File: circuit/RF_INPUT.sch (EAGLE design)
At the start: 90 parts, among them IC1 TS464, IC2 SN74LVC1G3157DBVR, U1 SA612, U2 SA612, U3 SA612, X1 BU-SMA-V, X4 SMA-142-0701-801/806, X5 BU-SMA-V, X6 SMA-142-0701-801/806

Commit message: - развели половину
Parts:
- removed C37: nc, rcl:C-EUC0603
- removed R10: 680K, rcl:R-EU_R0603
- C1, C10, C11, C15, C18, C19, C20, C21, C22, C23, C26, C31, C32, C33, C34, C4, C6, C7, C8: device rcl:C-EUC0603 -> rcl:C-EUC0805
- C24: value 220N -> 100N
- C25: value nc -> 220N; device rcl:C-EUC0603 -> rcl:C-EUC0805
- R11: value 680K -> 330K
- R41: value 150K -> 330k
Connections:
- removed net LO_RX: U3.OSCB
- new net N$3: C25.2, U3.OSCB
- net +6V0: no longer R10.2
- net GND: now also C24.1; no longer C24.2, C25.2, C37.2, R11.2
- net LO_TX: now also C25.1
- net N$47: no longer C37.1
- net N$59: no longer C25.1
- net N$73: no longer R10.1
- net OPA_BIAS: now also C24.2, R11.2; no longer C24.1
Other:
- moved on the sheet: C24, C25, R11

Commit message: - почти разведенная схема
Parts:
- added Q1, Q2: IRML6302, transistor-small-signal:BSS84
- added R10, R42: 4.7k, rcl:R-EU_R0603
- added R43, R44: 68k, rcl:R-EU_R0603
- added R45: 220, rcl:R-EU_R0603
- added X8: (no value), con-phoenix-254:MPT2
- C30: device rcl:C-EUC0603 -> rcl:C-EUC0805
- R14, R19, R2, R21, R3: device rcl:R-EU_R0603 -> rcl:R-EU_R0805
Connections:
- new net N$10: R10.1, X8-1.1
- new net N$11: IC2.B2, R45.2
- new net N$4: C26.1, C27.1, Q2.D, U3.VCC
- new net N$6: Q1.G, R10.2, R43.2
- new net N$7: Q2.G, R42.2, R44.2
- new net N$8: C15.1, C16.1, Q1.D, U2.VCC
- new net N$9: R42.1, X8-2.1
- net +6V0: now also Q1.S, Q2.S, R43.1, R44.1; no longer C15.1, C16.1, C26.1, C27.1, U2.VCC, U3.VCC
- net ADC_SWITCH_CNTRL: now also IC2.A; no longer R36.2
- net ADC_SWITCH_NC: now also IC1A.OUT, R45.1; no longer IC1B.OUT, IC2.B2
- net ADC_SWITCH_NO: now also R36.1; no longer IC2.B1
- net ADC_SWITCH_NO2: now also IC1B.OUT; no longer IC1A.OUT
- net N$2: now also IC2.B1, R36.2; no longer IC2.A, R36.1
- net N$55: now also IC1A.-IN; no longer IC1B.-IN
- net N$59: now also IC1A.+IN; no longer IC1B.+IN
- net N$69: now also IC1B.-IN; no longer IC1A.-IN
- net N$73: now also IC1B.+IN; no longer IC1A.+IN
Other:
- moved on the sheet: C26, C27, IC1A, IC1B, IC1D, R36

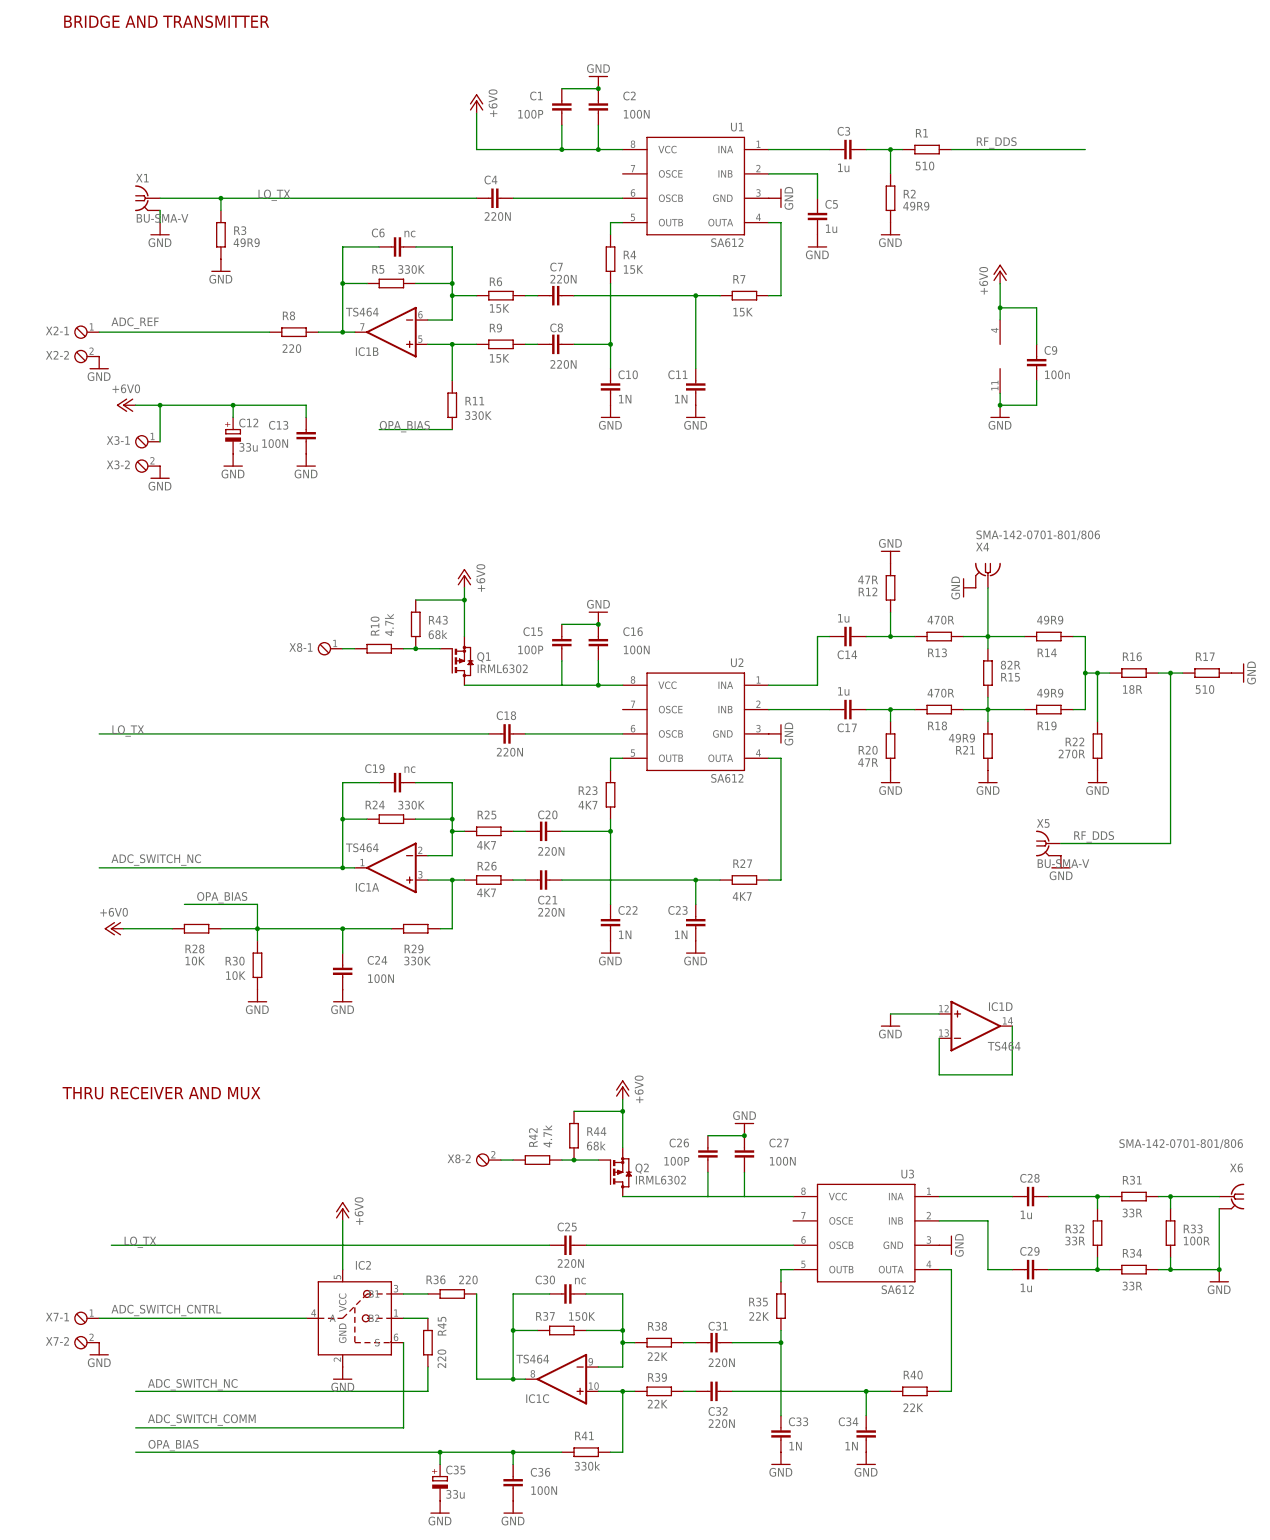
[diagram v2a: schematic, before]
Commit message: - добавили транзистор, чтобы переключалось одной линией. - индуктивность на питание
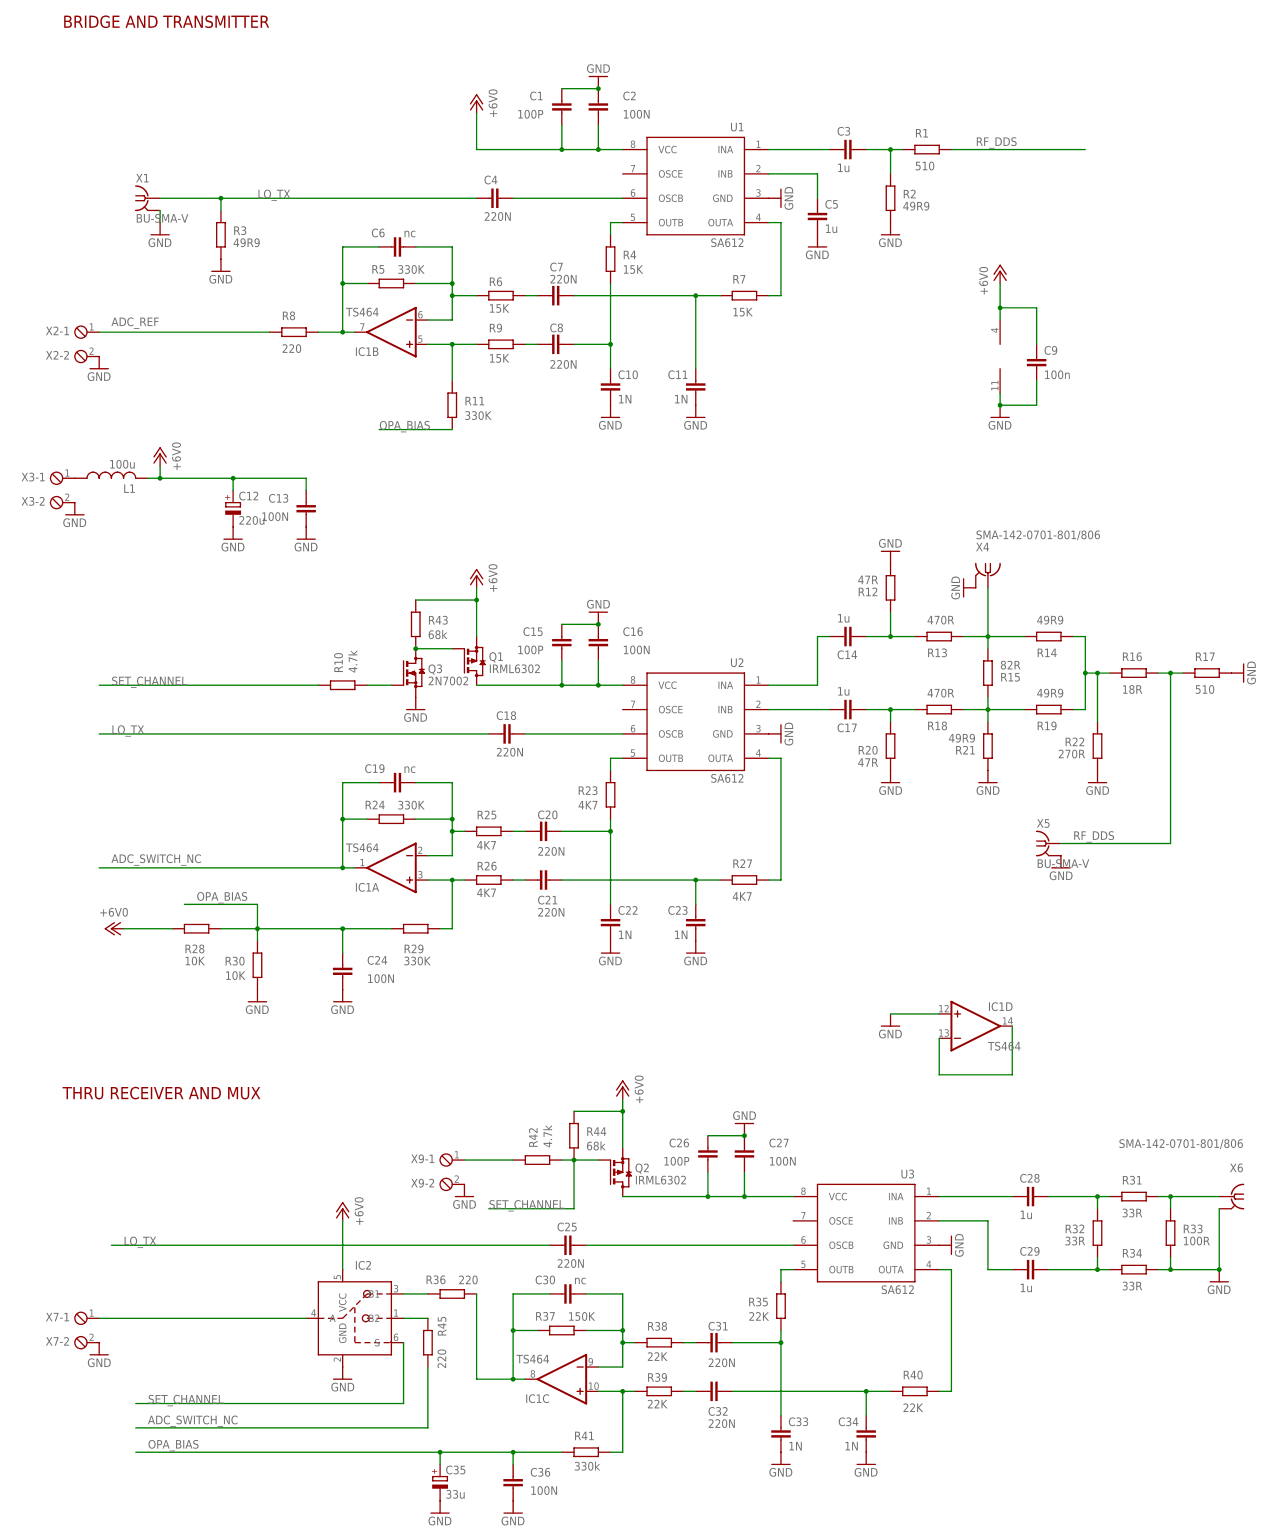
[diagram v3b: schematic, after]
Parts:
- removed X8: (no value), con-phoenix-254:MPT2
- added L1: 100u, rcl:L-US0207/12
- added Q3: 2N7002, transistor-small-signal:BSS123
- added X9: (no value), con-phoenix-254:MPT2
- C12: value 33u -> 220u
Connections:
- net ADC_SWITCH_CNTRL renamed N$12
- removed net ADC_SWITCH_COMM: IC2.S
- removed net N$10: R10.1, X8-1.1
- new net N$14: Q3.G, R10.2
- new net SET_CHANNEL: IC2.S, Q2.G, R10.1, R42.2, R44.2
- net +6V0: now also L1.2; no longer X3-1.1
- net GND: now also Q3.S, X9-2.1
- net N$6: now also Q3.D; no longer R10.2
- net N$7: now also L1.1, X3-1.1; no longer Q2.G, R42.2, R44.2
- net N$9: now also X9-1.1; no longer X8-2.1
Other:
- moved on the sheet: C12, C13, Q1, R10, X3-1, X3-2

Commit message: - работающий в первом приближении USB Virtual Com Port
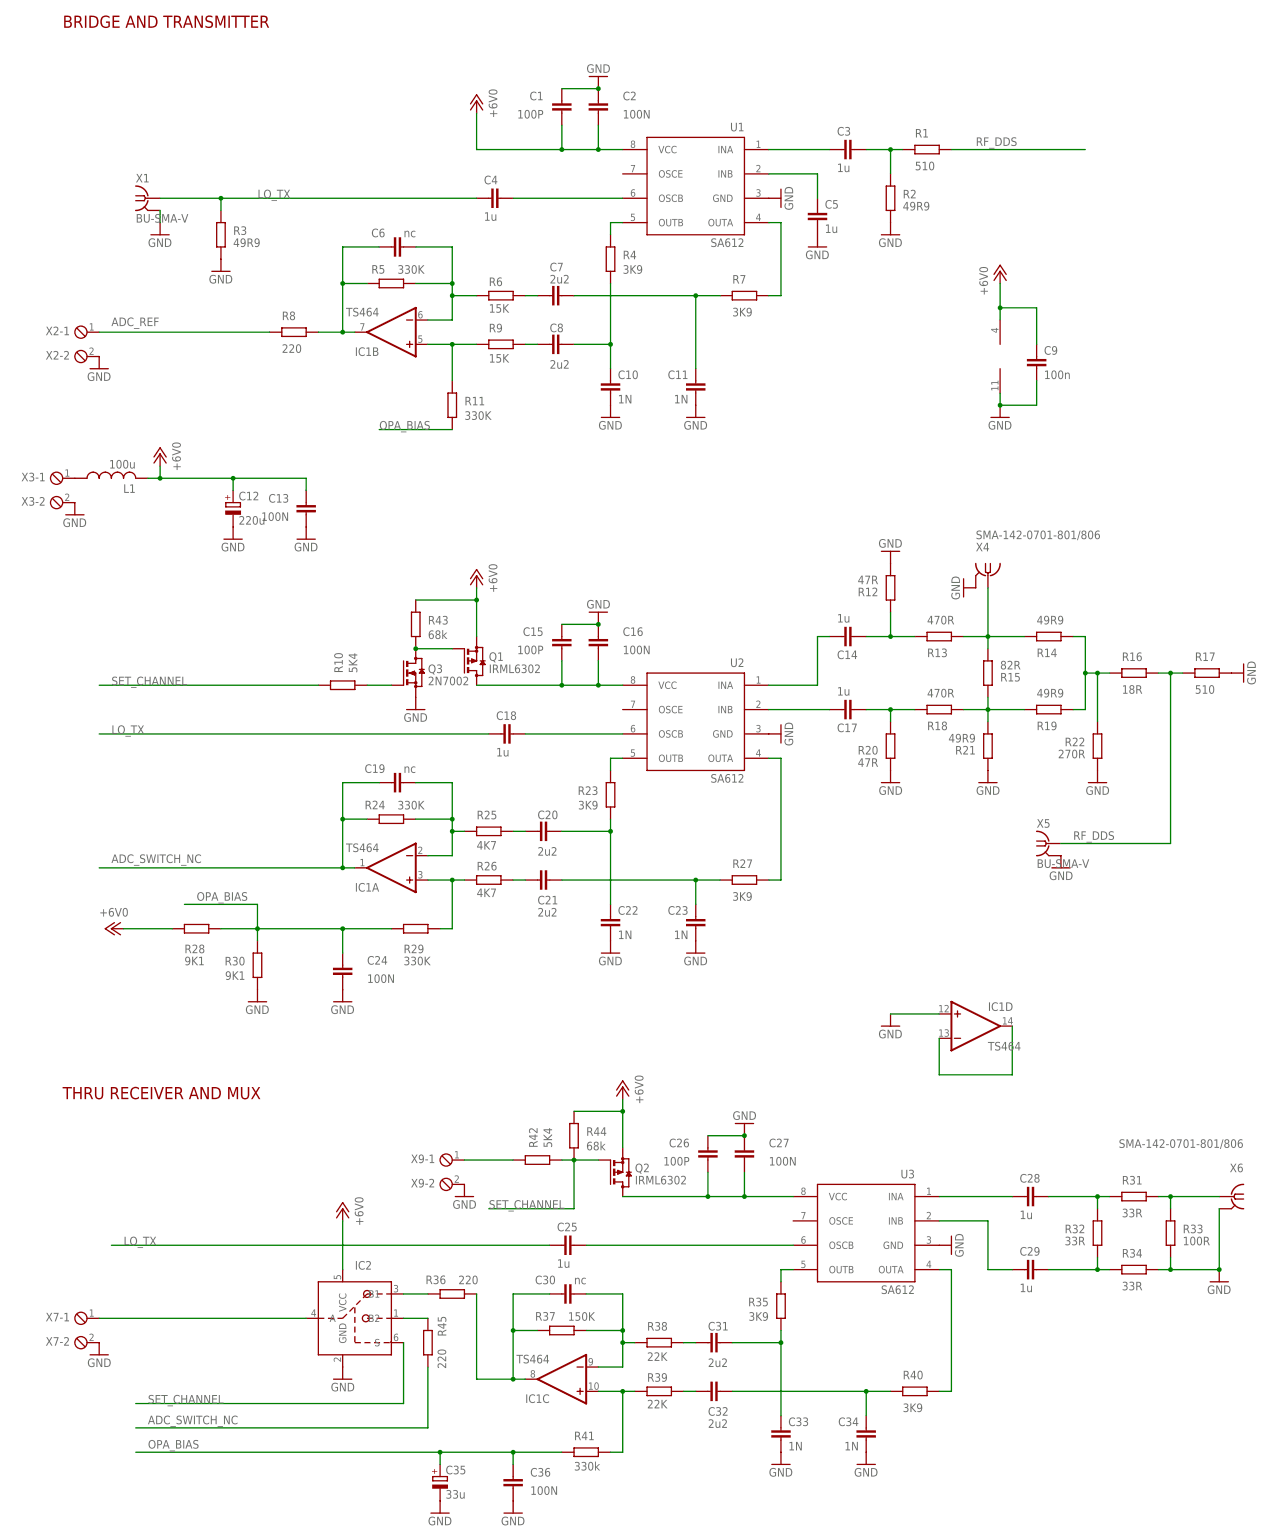
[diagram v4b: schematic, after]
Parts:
- C18, C25, C4: value 220N -> 1u
- C20, C21, C31, C32, C7, C8: value 220N -> 2u2
- R10, R42: value 4.7k -> 5K4
- R23, R27: value 4K7 -> 3K9
- R28, R30: value 10K -> 9K1
- R35, R40: value 22K -> 3K9
- R4, R7: value 15K -> 3K9
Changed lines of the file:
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@@
 <part name="C29" library="rcl" deviceset="C-EU" device="C0603" value="1u"/>
 <part name="GND31" library="supply1" deviceset="GND" device=""/>
-<part name="R40" library="rcl" deviceset="R-EU_" device="R0603" value="22K"/>
-<part name="R35" library="rcl" deviceset="R-EU_" device="R0603" value="22K"/>
+<part name="R40" library="rcl" deviceset="R-EU_" device="R0603" value="3K9"/>
+<part name="R35" library="rcl" deviceset="R-EU_" device="R0603" value="3K9"/>
 <part name="C34" library="rcl" deviceset="C-EU" device="C0805" value="1N"/>
 <part name="C33" library="rcl" deviceset="C-EU" device="C0805" value="1N"/>
 <part name="GND36" library="supply1" deviceset="GND" device=""/>
 <part name="GND35" library="supply1" deviceset="GND" device=""/>
-<part name="C32" library="rcl" deviceset="C-EU" device="C0805" value="220N"/>
-<part name="C31" library="rcl" deviceset="C-EU" device="C0805" value="220N"/>
+<part name="C32" library="rcl" deviceset="C-EU" device="C0805" value="2u2"/>
+<part name="C31" library="rcl" deviceset="C-EU" device="C0805" value="2u2"/>
 <part name="C27" library="rcl" deviceset="C-EU" device="C0603" value="100N"/>
 <part name="C26" library="rcl" deviceset="C-EU" device="C0805" value="100P"/>
@@
 <part name="C14" library="rcl" deviceset="C-EU" device="C0603" value="1u"/>
 <part name="GND19" library="supply1" deviceset="GND" device=""/>
-<part name="R27" library="rcl" deviceset="R-EU_" device="R0603" value="4K7"/>
-<part name="R23" library="rcl" deviceset="R-EU_" device="R0603" value="4K7"/>
+<part name="R27" library="rcl" deviceset="R-EU_" device="R0603" value="3K9"/>
+<part name="R23" library="rcl" deviceset="R-EU_" device="R0603" value="3K9"/>
 <part name="C23" library="rcl" deviceset="C-EU" device="C0805" value="1N"/>
 <part name="C22" library="rcl" deviceset="C-EU" device="C0805" value="1N"/>
 <part name="GND25" library="supply1" deviceset="GND" device=""/>
 <part name="GND24" library="supply1" deviceset="GND" device=""/>
-<part name="C21" library="rcl" deviceset="C-EU" device="C0805" value="220N"/>
-<part name="C20" library="rcl" deviceset="C-EU" device="C0805" value="220N"/>
+<part name="C21" library="rcl" deviceset="C-EU" device="C0805" value="2u2"/>
+<part name="C20" library="rcl" deviceset="C-EU" device="C0805" value="2u2"/>
 <part name="C16" library="rcl" deviceset="C-EU" device="C0603" value="100N"/>
 <part name="C15" library="rcl" deviceset="C-EU" device="C0805" value="100P"/>
@@
 <part name="R29" library="rcl" deviceset="R-EU_" device="R0603" value="330K"/>
 <part name="GND27" library="supply1" deviceset="GND" device=""/>
-<part name="R28" library="rcl" deviceset="R-EU_" device="R0603" value="10K"/>
+<part name="R28" library="rcl" deviceset="R-EU_" device="R0603" value="9K1"/>
 <part name="GND10" library="supply1" deviceset="GND" device=""/>
 <part name="R8" library="rcl" deviceset="R-EU_" device="R0603" value="220"/>
@@
 <part name="GND21" library="supply1" deviceset="GND" device=""/>
 <part name="R3" library="rcl" deviceset="R-EU_" device="R0805" value="49R9"/>
-<part name="C18" library="rcl" deviceset="C-EU" device="C0805" value="220N"/>
+<part name="C18" library="rcl" deviceset="C-EU" device="C0805" value="1u"/>
 <part name="GND6" library="supply1" deviceset="GND" device=""/>
 <part name="U1" library="vnwa" deviceset="SA612" device=""/>
@@
 <part name="C3" library="rcl" deviceset="C-EU" device="C0603" value="1u"/>
 <part name="GND2" library="supply1" deviceset="GND" device=""/>
-<part name="R7" library="rcl" deviceset="R-EU_" device="R0603" value="15K"/>
-<part name="R4" library="rcl" deviceset="R-EU_" device="R0603" value="15K"/>
+<part name="R7" library="rcl" deviceset="R-EU_" device="R0603" value="3K9"/>
+<part name="R4" library="rcl" deviceset="R-EU_" device="R0603" value="3K9"/>
 <part name="C11" library="rcl" deviceset="C-EU" device="C0805" value="1N"/>
 <part name="C10" library="rcl" deviceset="C-EU" device="C0805" value="1N"/>
 <part name="GND9" library="supply1" deviceset="GND" device=""/>
 <part name="GND8" library="supply1" deviceset="GND" device=""/>
-<part name="C7" library="rcl" deviceset="C-EU" device="C0805" value="220N"/>
-<part name="C8" library="rcl" deviceset="C-EU" device="C0805" value="220N"/>
+<part name="C7" library="rcl" deviceset="C-EU" device="C0805" value="2u2"/>
+<part name="C8" library="rcl" deviceset="C-EU" device="C0805" value="2u2"/>
 <part name="C2" library="rcl" deviceset="C-EU" device="C0603" value="100N"/>
 <part name="C1" library="rcl" deviceset="C-EU" device="C0805" value="100P"/>
@@
 <part name="GND5" library="supply1" deviceset="GND" device=""/>
 <part name="GND4" library="supply1" deviceset="GND" device=""/>
-<part name="C4" library="rcl" deviceset="C-EU" device="C0805" value="220N"/>
+<part name="C4" library="rcl" deviceset="C-EU" device="C0805" value="1u"/>
 <part name="C5" library="rcl" deviceset="C-EU" device="C0603" value="1u"/>
 <part name="C9" library="rcl" deviceset="C-EU" device="C0603" value="100n"/>
-<part name="R30" library="rcl" deviceset="R-EU_" device="R0603" value="10K"/>
+<part name="R30" library="rcl" deviceset="R-EU_" device="R0603" value="9K1"/>
 <part name="GND26" library="supply1" deviceset="GND" device=""/>
 <part name="P+1" library="vnwa" deviceset="+6V0" device=""/>
@@
 <part name="GND7" library="supply1" deviceset="GND" device=""/>
 <part name="C24" library="rcl" deviceset="C-EU" device="C0603" value="100N"/>
-<part name="C25" library="rcl" deviceset="C-EU" device="C0805" value="220N"/>
+<part name="C25" library="rcl" deviceset="C-EU" device="C0805" value="1u"/>
 <part name="Q1" library="transistor-small-signal" deviceset="BSS84" device="" value="IRML6302"/>
-<part name="R10" library="rcl" deviceset="R-EU_" device="R0603" value="4.7k"/>
+<part name="R10" library="rcl" deviceset="R-EU_" device="R0603" value="5K4"/>
 <part name="Q2" library="transistor-small-signal" deviceset="BSS84" device="" value="IRML6302"/>
-<part name="R42" library="rcl" deviceset="R-EU_" device="R0603" value="4.7k"/>
+<part name="R42" library="rcl" deviceset="R-EU_" device="R0603" value="5K4"/>
 <part name="P+7" library="vnwa" deviceset="+6V0" device=""/>
 <part name="R43" library="rcl" deviceset="R-EU_" device="R0603" value="68k"/>

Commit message: - начали рисовать платку с дифференциальным входом.
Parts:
- X4, X6: value SMA-142-0701-801/806 -> SMA
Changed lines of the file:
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@@
 <?xml version="1.0" encoding="utf-8"?>
 <!DOCTYPE eagle SYSTEM "eagle.dtd">
-<eagle version="7.1.0">
+<eagle version="7.4.0">
 <drawing>
 <settings>
@@
 <parts>
 <part name="U3" library="vnwa" deviceset="SA612" device=""/>
-<part name="X4" library="con-coax" deviceset="SMA-" device="142-0701-801/806" value="SMA-142-0701-801/806"/>
-<part name="X6" library="con-coax" deviceset="SMA-" device="142-0701-801/806" value="SMA-142-0701-801/806"/>
+<part name="X4" library="con-coax" deviceset="SMA-" device="142-0701-801/806" value="SMA"/>
+<part name="X6" library="con-coax" deviceset="SMA-" device="142-0701-801/806" value="SMA"/>
 <part name="GND32" library="supply1" deviceset="GND" device=""/>
 <part name="R33" library="rcl" deviceset="R-EU_" device="R0603" value="100R"/>
